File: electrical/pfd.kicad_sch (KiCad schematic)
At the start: 15 parts

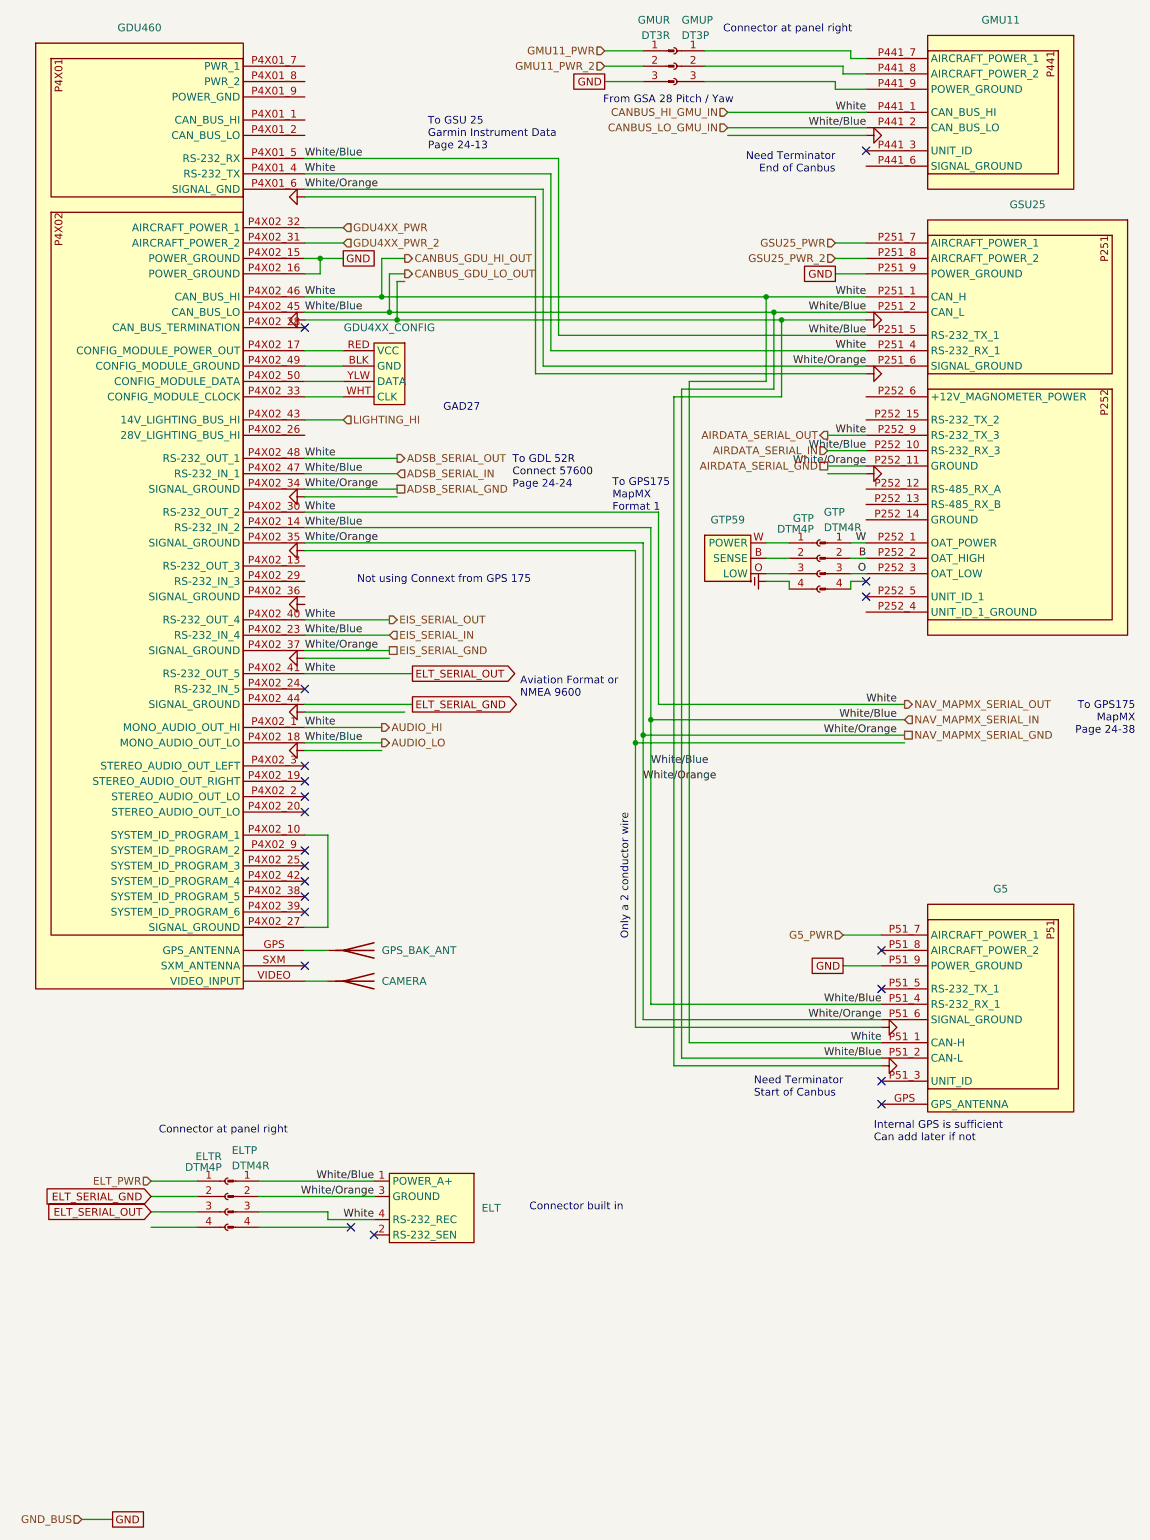
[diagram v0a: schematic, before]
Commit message: Upgraded G3X Touch to Axis
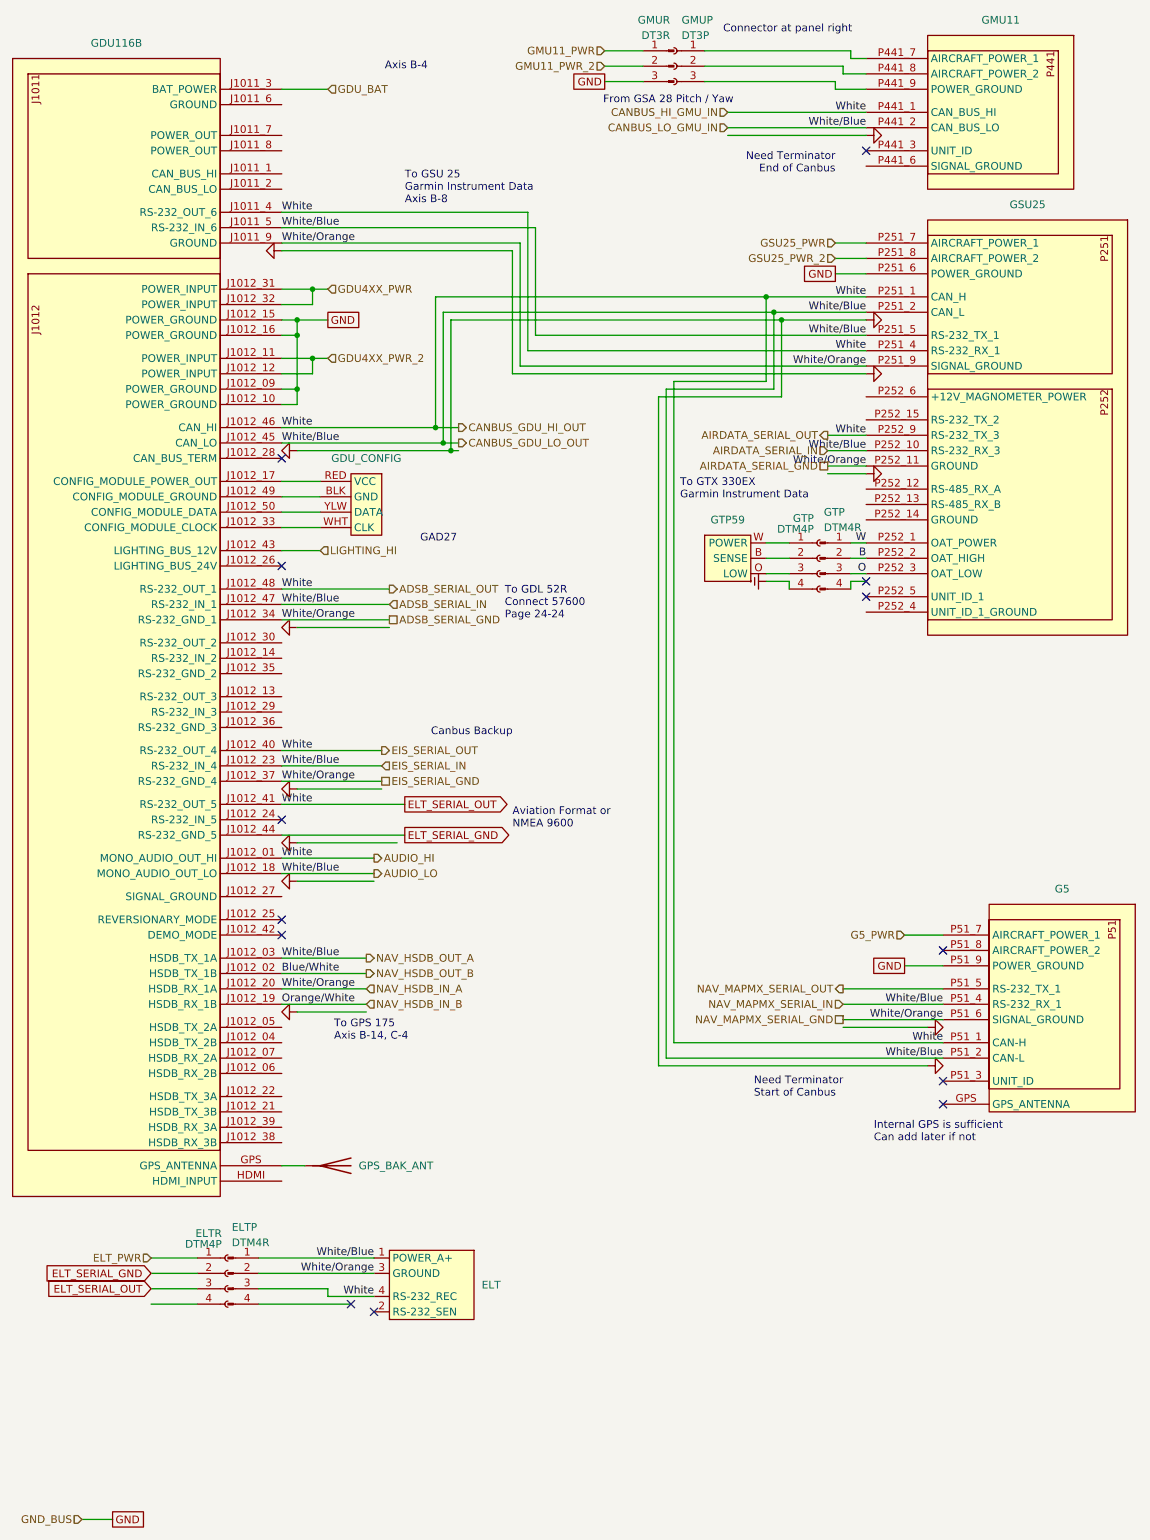
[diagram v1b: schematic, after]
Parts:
- removed CAMERA: Antenna, symbol Device:Antenna
- removed GDU460: ~, symbol flyerx:Garmin_GDU4XX
- added GDU116B: (no value), symbol flyerx:Garmin_GDU116B
- ELT, G5, GMU11, GSU25, GTP59: value ~ -> (none)
- GDU_CONFIG: renamed from GDU4XX_CONFIG; value ~ -> (none)
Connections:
- net ADSB_SERIAL_GND: now also GSU25.P251_9 (SIGNAL_GROUND), GDU116B.J1011_9 (GROUND), GDU116B.J1012_20 (HSDB_RX_1A), GDU116B.J1012_34 (RS-232_GND_1), GDU116B.J1012_37 (RS-232_GND_4); no longer GSU25.P251_6 (SIGNAL_GROUND)
- net ADSB_SERIAL_IN: now also GDU116B.J1011_5 (RS-232_IN_6), GDU116B.J1012_03 (HSDB_TX_1A), GDU116B.J1012_18 (MONO_AUDIO_OUT_LO), GDU116B.J1012_23 (RS-232_IN_4), GDU116B.J1012_45 (CAN_LO), GDU116B.J1012_47 (RS-232_IN_1)
- net ELT_SERIAL_GND: now also GDU116B.J1012_44 (RS-232_GND_5)
- net ELT_SERIAL_OUT: now also GDU116B.J1011_4 (RS-232_OUT_6), GDU116B.J1012_01 (MONO_AUDIO_OUT_HI), GDU116B.J1012_40 (RS-232_OUT_4), GDU116B.J1012_41 (RS-232_OUT_5), GDU116B.J1012_46 (CAN_HI), GDU116B.J1012_48 (RS-232_OUT_1)
- net GDU4XX_PWR: now also GDU116B.J1012_31 (POWER_INPUT), GDU116B.J1012_32 (POWER_INPUT)
- net GDU4XX_PWR_2: now also GDU116B.J1012_11 (POWER_INPUT), GDU116B.J1012_12 (POWER_INPUT)
- net GND: now also GSU25.P251_6 (POWER_GROUND), GDU116B.J1012_09 (POWER_GROUND), GDU116B.J1012_10 (POWER_GROUND), GDU116B.J1012_15 (POWER_GROUND), GDU116B.J1012_16 (POWER_GROUND); no longer GSU25.P251_9 (POWER_GROUND)
- net LIGHTING_HI: now also GDU116B.J1012_43 (LIGHTING_BUS_12V)
- net NAV_MAPMX_SERIAL_OUT: now reaches G5.P51_5 (RS-232_TX_1)
- net at GPS_BAK_ANT.1 (A): now also GDU116B.GPS (GPS_ANTENNA)
- net at GDU_CONFIG.BLK (GND): now also GDU116B.J1012_49 (CONFIG_MODULE_GROUND)
- net at GDU_CONFIG.RED (VCC): now also GDU116B.J1012_17 (CONFIG_MODULE_POWER_OUT)
- net at GDU_CONFIG.WHT (CLK): now also GDU116B.J1012_33 (CONFIG_MODULE_CLOCK)
- net at GDU_CONFIG.YLW (DATA): now also GDU116B.J1012_50 (CONFIG_MODULE_DATA)
- new net GDU_BAT: GDU116B.J1011_3 (BAT_POWER)
- new net NAV_HSDB_IN_B: GDU116B.J1012_19 (HSDB_RX_1B)
- new net NAV_HSDB_OUT_B: GDU116B.J1012_02 (HSDB_TX_1B)
- no-connect marks 21 -> 13
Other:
- note added: "Axis B-4"
- note added: "Canbus Backup"
- note added: "To GPS 175 Axis B-14, C-4"
- note added: "To GSU 25 Garmin Instrument Data Axis B-8"
- note added: "To GTX 330EX Garmin Instrument Data"
- note removed: "Connector built in"
- note removed: "Not using Connext from GPS 175"
- note removed: "Only a 2 conductor wire"
- note removed: "To GPS175 MapMX Format 1"
- note removed: "To GPS175 MapMX Page 24-38"
- note removed: "To GSU 25 Garmin Instrument Data Page 24-13"
- moved on the sheet: ELT, ELTP, ELTR, G5, GDU_CONFIG, GPS_BAK_ANT

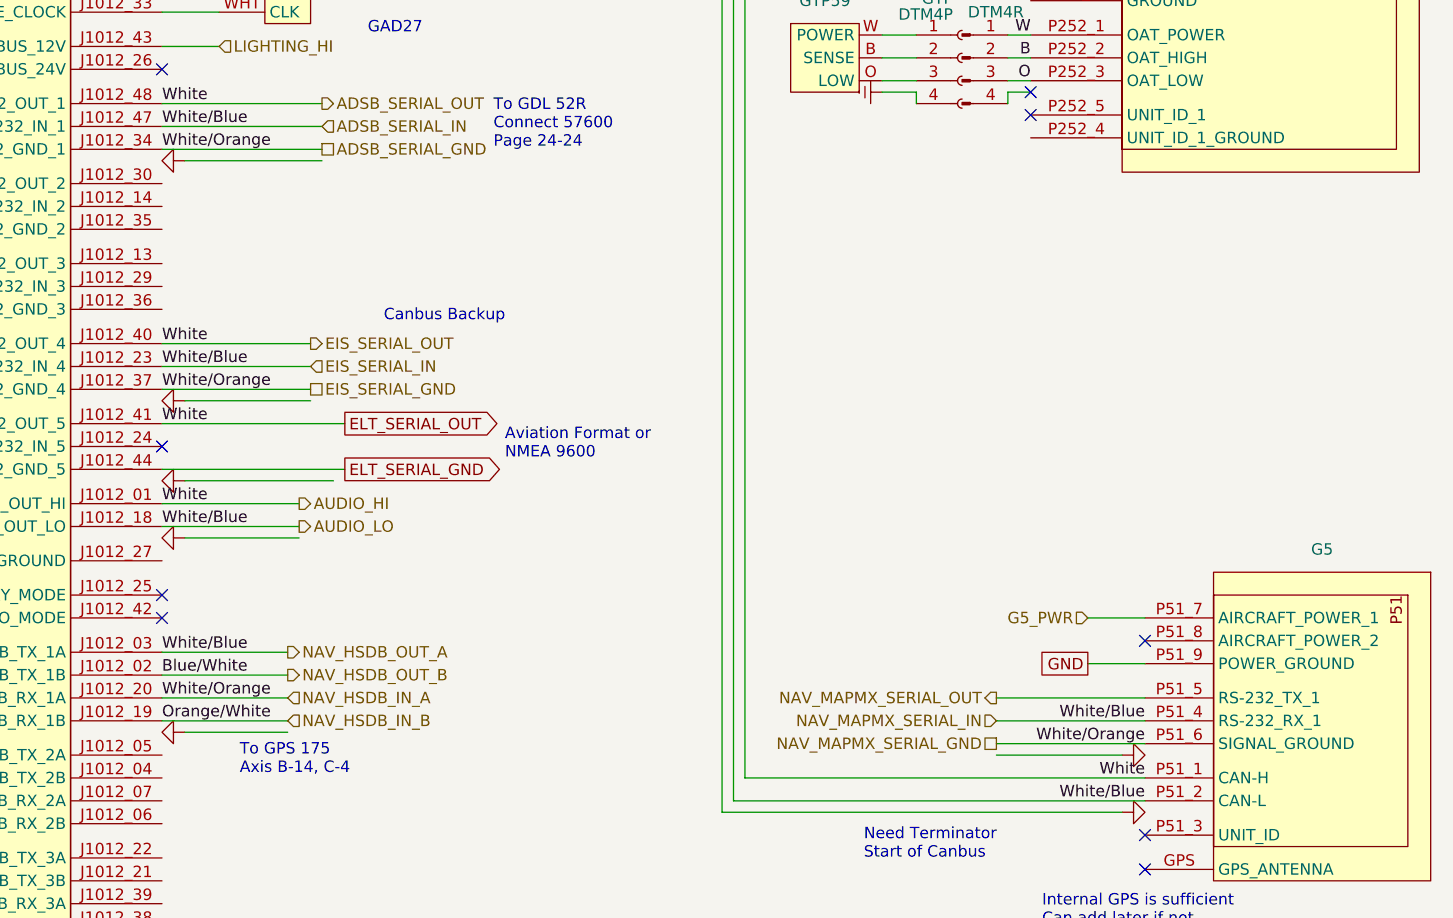
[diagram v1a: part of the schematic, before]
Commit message: Kept MapMX serial to GDU. It'll just be ignored anyways.
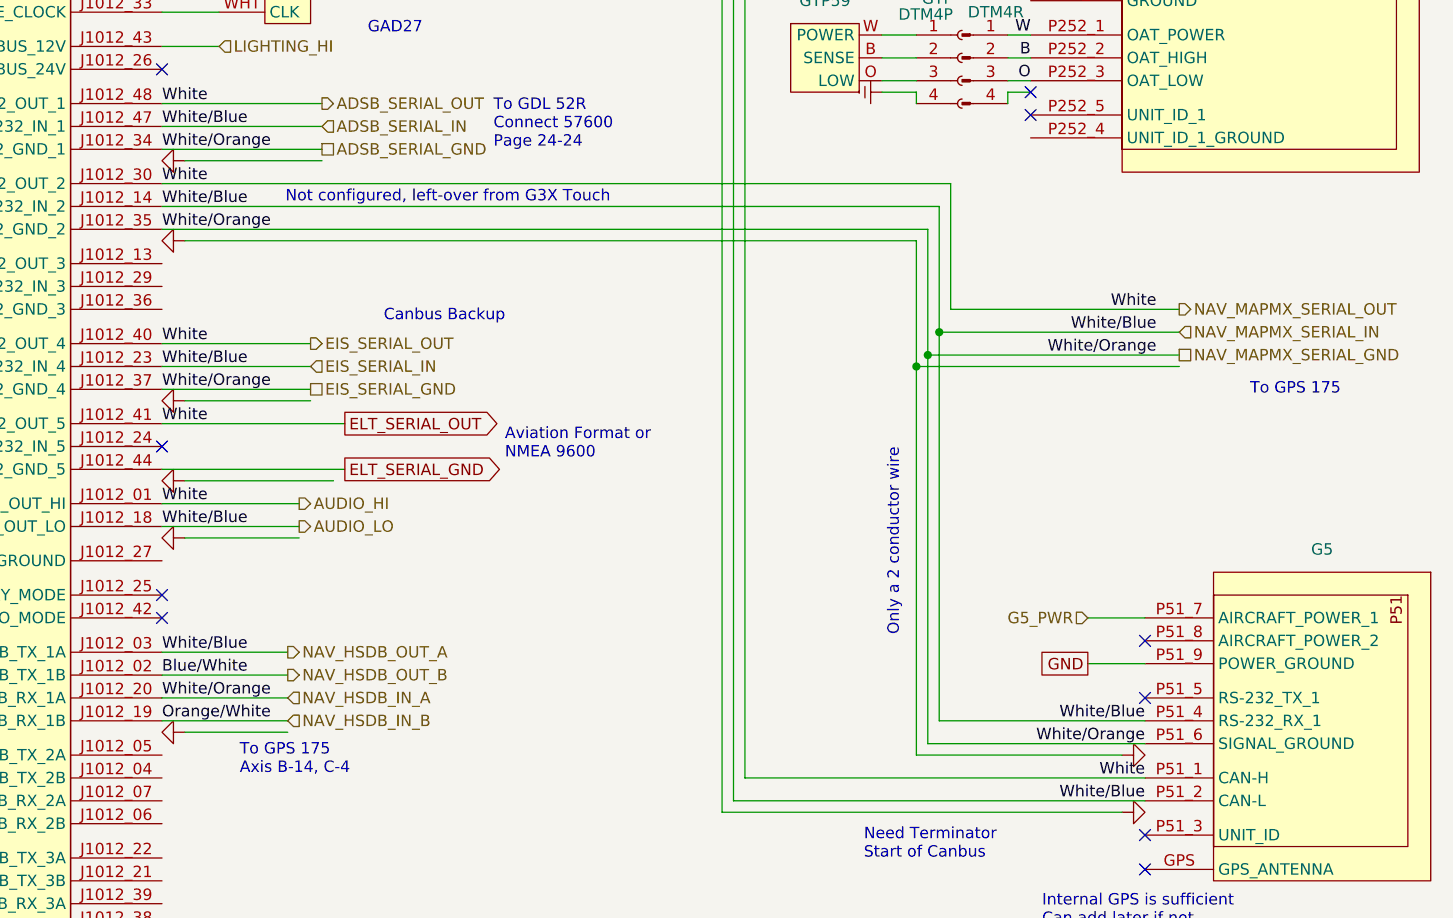
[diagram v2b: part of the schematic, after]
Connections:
- net ADSB_SERIAL_GND: now also GDU116B.J1012_35 (RS-232_GND_2)
- net ADSB_SERIAL_IN: now also GDU116B.J1012_14 (RS-232_IN_2)
- net ELT_SERIAL_OUT: now also GDU116B.J1012_30 (RS-232_OUT_2)
- net NAV_MAPMX_SERIAL_OUT: no longer names the net of G5.P51_5 (RS-232_TX_1)
- no-connect marks 13 -> 14
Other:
- note added: "Not configured, left-over from G3X Touch"
- note added: "Only a 2 conductor wire"
- note added: "To GPS 175"
